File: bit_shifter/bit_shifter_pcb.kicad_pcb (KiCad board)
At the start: 2 copper layers, 116.8 x 50.5 mm, 44 parts, among them J1 Conn_01x04, J2 Conn_02x08_Odd_Even, J3 Conn_02x02_Odd_Even, U1 74LS194, U2 74LS194, U3 74LS194, U4 74LS194, U5 74LS244, U6 74LS244

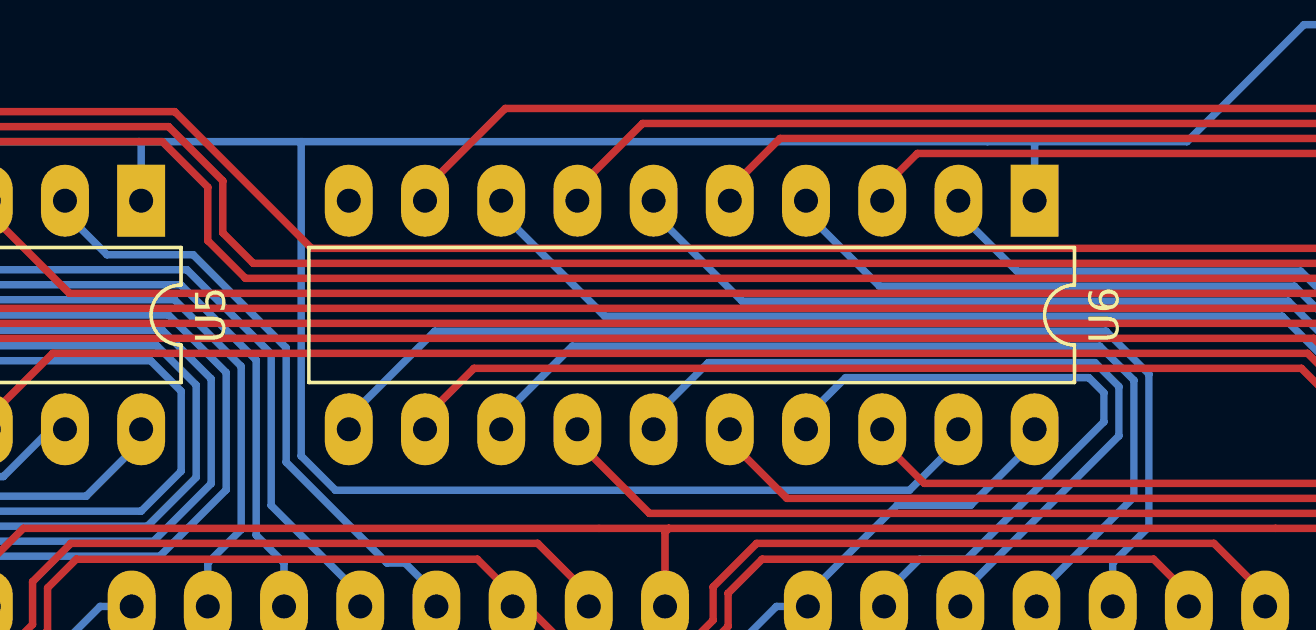
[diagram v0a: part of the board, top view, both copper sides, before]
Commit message: connect cu and start creating material csv
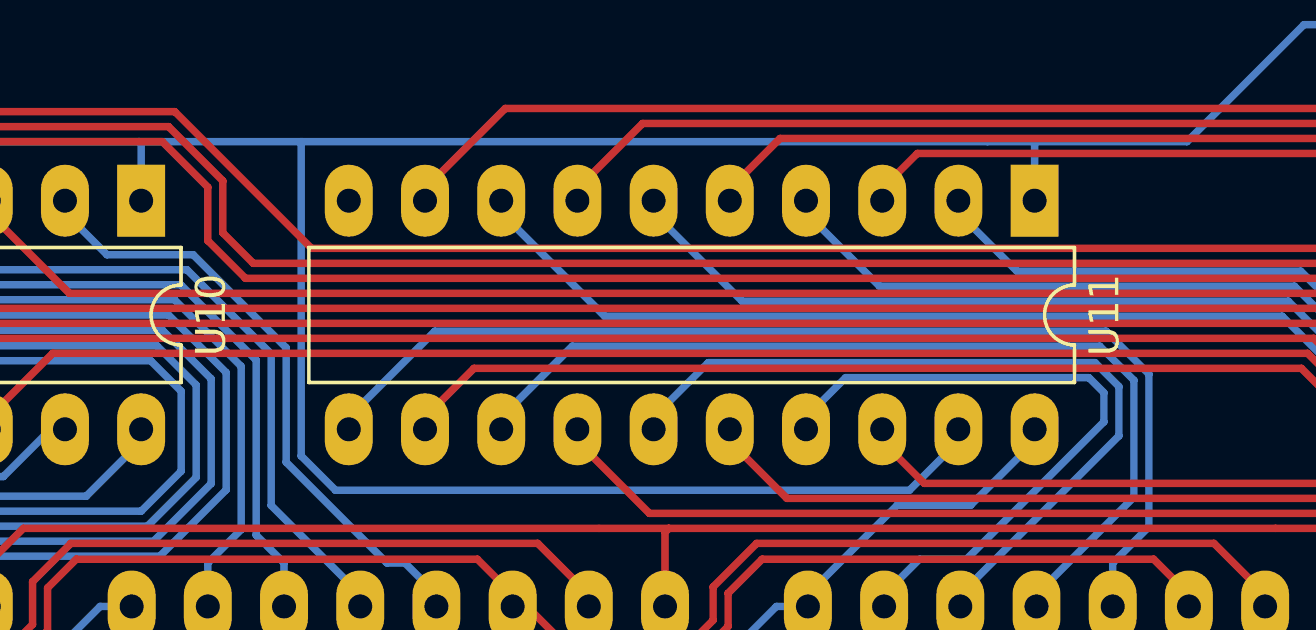
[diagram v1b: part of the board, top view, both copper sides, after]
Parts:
- renumbered U5 to U10, U6 to U11
